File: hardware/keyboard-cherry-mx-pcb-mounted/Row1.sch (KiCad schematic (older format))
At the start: 30 parts, among them SW15 `, SW16 8, SW17 1, SW18 9, SW19 2, SW20 0, SW21 3, SW22 -, SW23 4, SW24 =, SW25 5, SW26 Backspace, SW27 6, SW28 Home, SW29 7

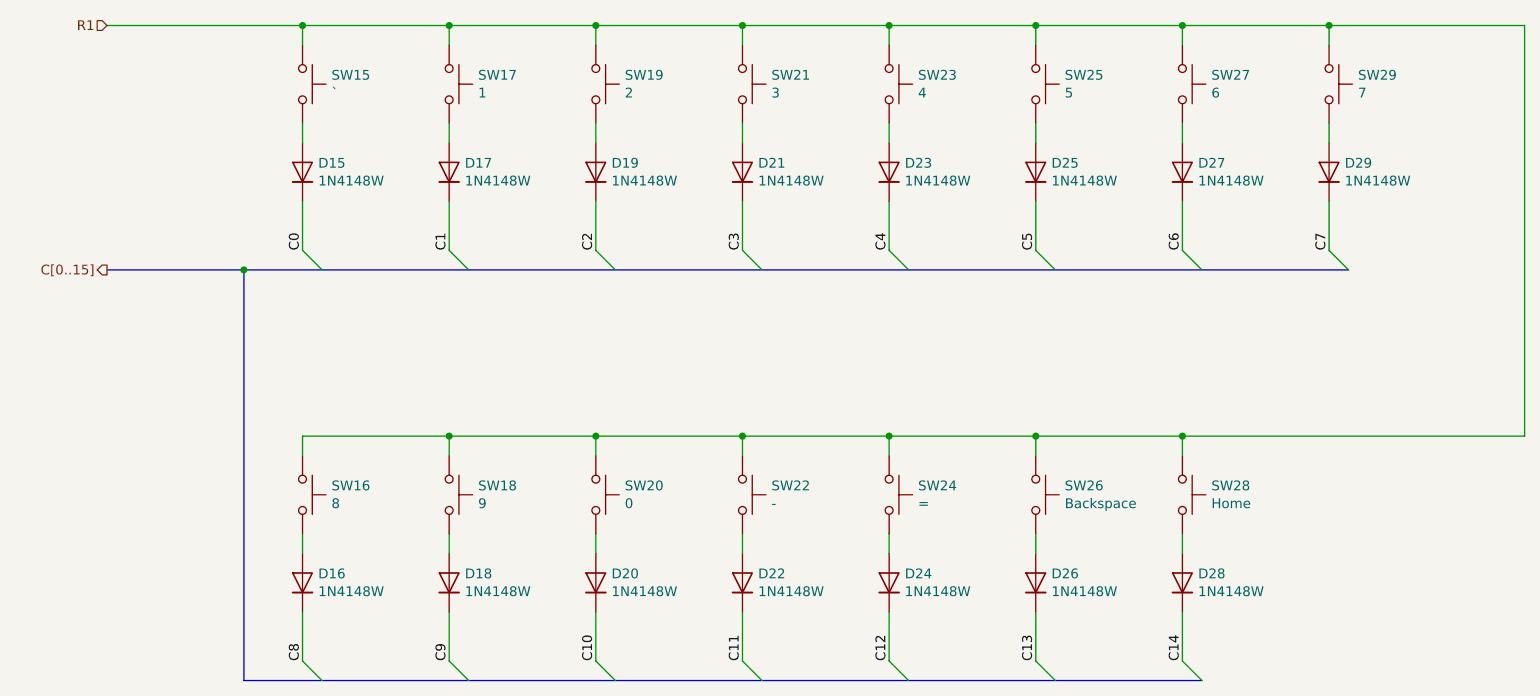
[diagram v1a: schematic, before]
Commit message: Adds completed sensor and power connections. Still need to add USB footprint then sch are done for version 1.0
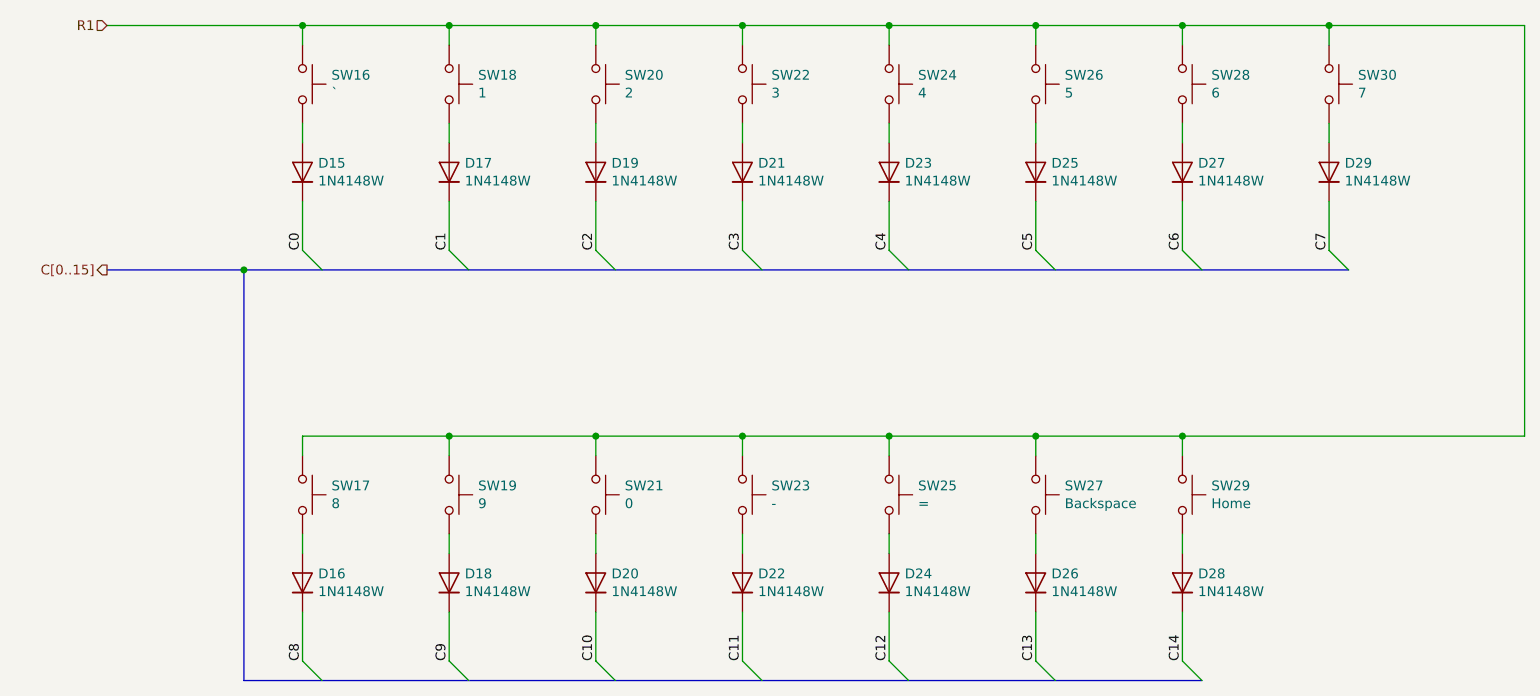
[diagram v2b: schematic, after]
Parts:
- renumbered SW15 to SW16, SW16 to SW17, SW17 to SW18, SW18 to SW19, SW19 to SW20, SW20 to SW21, SW21 to SW22, SW22 to SW23, SW23 to SW24, SW24 to SW25, SW25 to SW26, SW26 to SW27, SW27 to SW28, SW28 to SW29, SW29 to SW30
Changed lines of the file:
@@
 AR Path="/5E697948/5E775B33" Ref="SW?"  Part="1"
 AR Path="/5E697948/5E6CDE4B/5E775B33" Ref="SW?"  Part="1"
-AR Path="/5E697948/5E763FD4/5E775B33" Ref="SW15"  Part="1"
-F 0 "SW15" V 3154 2598 50  0000 L CNN
+AR Path="/5E697948/5E763FD4/5E775B33" Ref="SW16"  Part="1"
+F 0 "SW16" V 3154 2598 50  0000 L CNN
 F 1 "`" V 3245 2598 50  0000 L CNN
 F 2 "Button_Switch_Keyboard:SW_Cherry_MX_1.00u_PCB" H 3200 2650 50  0001 C CNN
@@
 AR Path="/5E697948/5E775B43" Ref="SW?"  Part="1"
 AR Path="/5E697948/5E6CDE4B/5E775B43" Ref="SW?"  Part="1"
-AR Path="/5E697948/5E763FD4/5E775B43" Ref="SW17"  Part="1"
-F 0 "SW17" V 3904 2598 50  0000 L CNN
+AR Path="/5E697948/5E763FD4/5E775B43" Ref="SW18"  Part="1"
+F 0 "SW18" V 3904 2598 50  0000 L CNN
 F 1 "1" V 3995 2598 50  0000 L CNN
 F 2 "Button_Switch_Keyboard:SW_Cherry_MX_1.00u_PCB" H 3950 2650 50  0001 C CNN
@@
 AR Path="/5E697948/5E775B51" Ref="SW?"  Part="1"
 AR Path="/5E697948/5E6CDE4B/5E775B51" Ref="SW?"  Part="1"
-AR Path="/5E697948/5E763FD4/5E775B51" Ref="SW19"  Part="1"
-F 0 "SW19" V 4654 2598 50  0000 L CNN
+AR Path="/5E697948/5E763FD4/5E775B51" Ref="SW20"  Part="1"
+F 0 "SW20" V 4654 2598 50  0000 L CNN
 F 1 "2" V 4745 2598 50  0000 L CNN
 F 2 "Button_Switch_Keyboard:SW_Cherry_MX_1.00u_PCB" H 4700 2650 50  0001 C CNN
@@
 AR Path="/5E697948/5E775B5F" Ref="SW?"  Part="1"
 AR Path="/5E697948/5E6CDE4B/5E775B5F" Ref="SW?"  Part="1"
-AR Path="/5E697948/5E763FD4/5E775B5F" Ref="SW21"  Part="1"
-F 0 "SW21" V 5404 2598 50  0000 L CNN
+AR Path="/5E697948/5E763FD4/5E775B5F" Ref="SW22"  Part="1"
+F 0 "SW22" V 5404 2598 50  0000 L CNN
 F 1 "3" V 5495 2598 50  0000 L CNN
 F 2 "Button_Switch_Keyboard:SW_Cherry_MX_1.00u_PCB" H 5450 2650 50  0001 C CNN
@@
 AR Path="/5E697948/5E775B6D" Ref="SW?"  Part="1"
 AR Path="/5E697948/5E6CDE4B/5E775B6D" Ref="SW?"  Part="1"
-AR Path="/5E697948/5E763FD4/5E775B6D" Ref="SW23"  Part="1"
-F 0 "SW23" V 6154 2598 50  0000 L CNN
+AR Path="/5E697948/5E763FD4/5E775B6D" Ref="SW24"  Part="1"
+F 0 "SW24" V 6154 2598 50  0000 L CNN
 F 1 "4" V 6245 2598 50  0000 L CNN
 F 2 "Button_Switch_Keyboard:SW_Cherry_MX_1.00u_PCB" H 6200 2650 50  0001 C CNN
@@
 AR Path="/5E697948/5E775B7B" Ref="SW?"  Part="1"
 AR Path="/5E697948/5E6CDE4B/5E775B7B" Ref="SW?"  Part="1"
-AR Path="/5E697948/5E763FD4/5E775B7B" Ref="SW25"  Part="1"
-F 0 "SW25" V 6904 2598 50  0000 L CNN
+AR Path="/5E697948/5E763FD4/5E775B7B" Ref="SW26"  Part="1"
+F 0 "SW26" V 6904 2598 50  0000 L CNN
 F 1 "5" V 6995 2598 50  0000 L CNN
 F 2 "Button_Switch_Keyboard:SW_Cherry_MX_1.00u_PCB" H 6950 2650 50  0001 C CNN
@@
 AR Path="/5E697948/5E775B89" Ref="SW?"  Part="1"
 AR Path="/5E697948/5E6CDE4B/5E775B89" Ref="SW?"  Part="1"
-AR Path="/5E697948/5E763FD4/5E775B89" Ref="SW27"  Part="1"
-F 0 "SW27" V 7654 2598 50  0000 L CNN
+AR Path="/5E697948/5E763FD4/5E775B89" Ref="SW28"  Part="1"
+F 0 "SW28" V 7654 2598 50  0000 L CNN
 F 1 "6" V 7745 2598 50  0000 L CNN
 F 2 "Button_Switch_Keyboard:SW_Cherry_MX_1.00u_PCB" H 7700 2650 50  0001 C CNN
@@
 AR Path="/5E697948/5E775B97" Ref="SW?"  Part="1"
 AR Path="/5E697948/5E6CDE4B/5E775B97" Ref="SW?"  Part="1"
-AR Path="/5E697948/5E763FD4/5E775B97" Ref="SW29"  Part="1"
-F 0 "SW29" V 8404 2598 50  0000 L CNN
+AR Path="/5E697948/5E763FD4/5E775B97" Ref="SW30"  Part="1"
+F 0 "SW30" V 8404 2598 50  0000 L CNN
 F 1 "7" V 8495 2598 50  0000 L CNN
 F 2 "Button_Switch_Keyboard:SW_Cherry_MX_1.00u_PCB" H 8450 2650 50  0001 C CNN
@@
 AR Path="/5E697948/5E775BA5" Ref="SW?"  Part="1"
 AR Path="/5E697948/5E6CDE4B/5E775BA5" Ref="SW?"  Part="1"
-AR Path="/5E697948/5E763FD4/5E775BA5" Ref="SW16"  Part="1"
-F 0 "SW16" V 3154 4698 50  0000 L CNN
+AR Path="/5E697948/5E763FD4/5E775BA5" Ref="SW17"  Part="1"
+F 0 "SW17" V 3154 4698 50  0000 L CNN
 F 1 "8" V 3245 4698 50  0000 L CNN
 F 2 "Button_Switch_Keyboard:SW_Cherry_MX_1.00u_PCB" H 3200 4750 50  0001 C CNN
@@
 AR Path="/5E697948/5E775BB3" Ref="SW?"  Part="1"
 AR Path="/5E697948/5E6CDE4B/5E775BB3" Ref="SW?"  Part="1"
-AR Path="/5E697948/5E763FD4/5E775BB3" Ref="SW18"  Part="1"
-F 0 "SW18" V 3904 4698 50  0000 L CNN
+AR Path="/5E697948/5E763FD4/5E775BB3" Ref="SW19"  Part="1"
+F 0 "SW19" V 3904 4698 50  0000 L CNN
 F 1 "9" V 3995 4698 50  0000 L CNN
 F 2 "Button_Switch_Keyboard:SW_Cherry_MX_1.00u_PCB" H 3950 4750 50  0001 C CNN
@@
 AR Path="/5E697948/5E775BC1" Ref="SW?"  Part="1"
 AR Path="/5E697948/5E6CDE4B/5E775BC1" Ref="SW?"  Part="1"
-AR Path="/5E697948/5E763FD4/5E775BC1" Ref="SW20"  Part="1"
-F 0 "SW20" V 4654 4698 50  0000 L CNN
+AR Path="/5E697948/5E763FD4/5E775BC1" Ref="SW21"  Part="1"
+F 0 "SW21" V 4654 4698 50  0000 L CNN
 F 1 "0" V 4745 4698 50  0000 L CNN
 F 2 "Button_Switch_Keyboard:SW_Cherry_MX_1.00u_PCB" H 4700 4750 50  0001 C CNN
@@
 AR Path="/5E697948/5E775BCF" Ref="SW?"  Part="1"
 AR Path="/5E697948/5E6CDE4B/5E775BCF" Ref="SW?"  Part="1"
-AR Path="/5E697948/5E763FD4/5E775BCF" Ref="SW22"  Part="1"
-F 0 "SW22" V 5404 4698 50  0000 L CNN
+AR Path="/5E697948/5E763FD4/5E775BCF" Ref="SW23"  Part="1"
+F 0 "SW23" V 5404 4698 50  0000 L CNN
 F 1 "-" V 5495 4698 50  0000 L CNN
 F 2 "Button_Switch_Keyboard:SW_Cherry_MX_1.00u_PCB" H 5450 4750 50  0001 C CNN
@@
 AR Path="/5E697948/5E775BDD" Ref="SW?"  Part="1"
 AR Path="/5E697948/5E6CDE4B/5E775BDD" Ref="SW?"  Part="1"
-AR Path="/5E697948/5E763FD4/5E775BDD" Ref="SW24"  Part="1"
-F 0 "SW24" V 6154 4698 50  0000 L CNN
+AR Path="/5E697948/5E763FD4/5E775BDD" Ref="SW25"  Part="1"
+F 0 "SW25" V 6154 4698 50  0000 L CNN
 F 1 "=" V 6245 4698 50  0000 L CNN
 F 2 "Button_Switch_Keyboard:SW_Cherry_MX_1.00u_PCB" H 6200 4750 50  0001 C CNN
@@
 AR Path="/5E697948/5E775BEB" Ref="SW?"  Part="1"
 AR Path="/5E697948/5E6CDE4B/5E775BEB" Ref="SW?"  Part="1"
-AR Path="/5E697948/5E763FD4/5E775BEB" Ref="SW26"  Part="1"
-F 0 "SW26" V 6904 4698 50  0000 L CNN
+AR Path="/5E697948/5E763FD4/5E775BEB" Ref="SW27"  Part="1"
+F 0 "SW27" V 6904 4698 50  0000 L CNN
 F 1 "Backspace" V 6995 4698 50  0000 L CNN
 F 2 "Button_Switch_Keyboard:SW_Cherry_MX_2.00u_PCB" H 6950 4750 50  0001 C CNN
@@
 AR Path="/5E697948/5E775BF9" Ref="SW?"  Part="1"
 AR Path="/5E697948/5E6CDE4B/5E775BF9" Ref="SW?"  Part="1"
-AR Path="/5E697948/5E763FD4/5E775BF9" Ref="SW28"  Part="1"
-F 0 "SW28" V 7654 4698 50  0000 L CNN
+AR Path="/5E697948/5E763FD4/5E775BF9" Ref="SW29"  Part="1"
+F 0 "SW29" V 7654 4698 50  0000 L CNN
 F 1 "Home" V 7745 4698 50  0000 L CNN
 F 2 "Button_Switch_Keyboard:SW_Cherry_MX_1.00u_PCB" H 7700 4750 50  0001 C CNN

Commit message: Aligns the keys so the column connections are more consistent. e.g. right most keys will have same column connection.
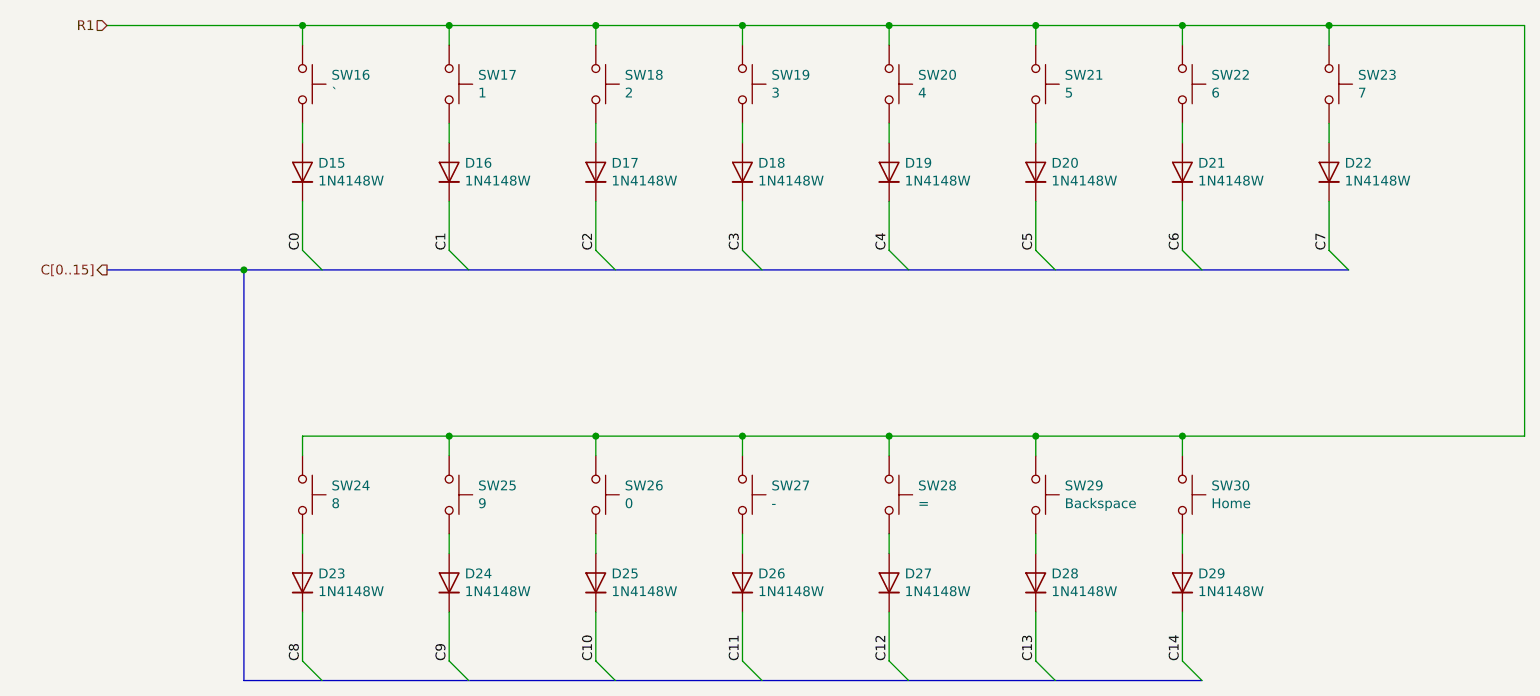
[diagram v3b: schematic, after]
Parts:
- renumbered D17 to D16, D19 to D17, D21 to D18, D23 to D19, D25 to D20, D27 to D21, D29 to D22, D16 to D23, D18 to D24, D20 to D25, D22 to D26, D24 to D27, D26 to D28, D28 to D29, SW18 to SW17, SW20 to SW18, SW22 to SW19, SW24 to SW20, SW26 to SW21, SW28 to SW22, SW30 to SW23, SW17 to SW24, SW19 to SW25, SW21 to SW26, SW23 to SW27, SW25 to SW28, SW27 to SW29, SW29 to SW30

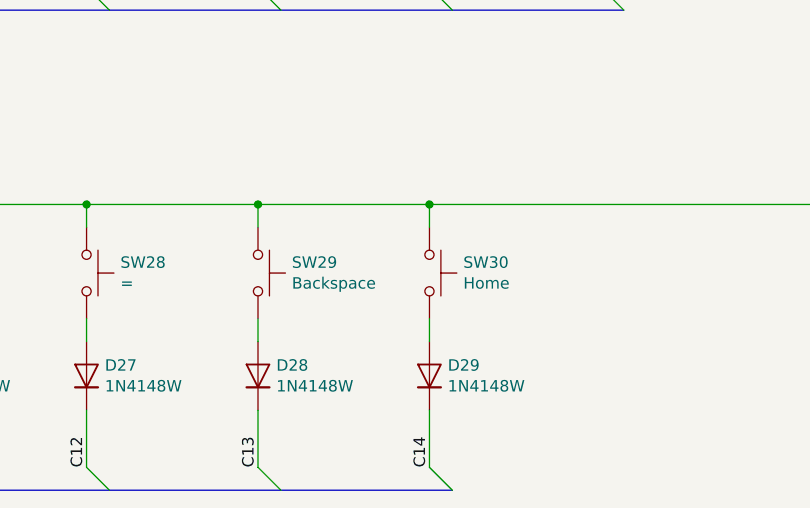
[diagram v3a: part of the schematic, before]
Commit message: Adds labels for each key and creates gerber files.
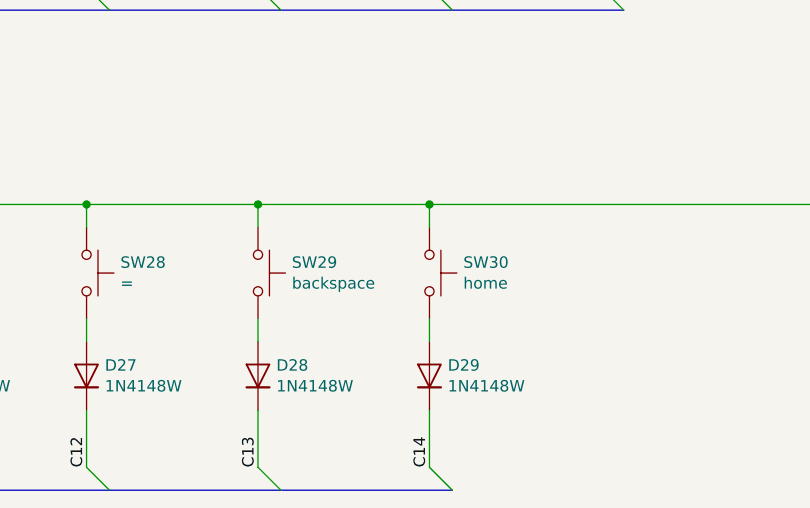
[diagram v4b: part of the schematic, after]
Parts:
- SW29: value Backspace -> backspace
- SW30: value Home -> home
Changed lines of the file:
@@
 AR Path="/5E697948/5E763FD4/5E775BEB" Ref="SW29"  Part="1"
 F 0 "SW29" V 6904 4698 50  0000 L CNN
-F 1 "Backspace" V 6995 4698 50  0000 L CNN
+F 1 "backspace" V 6995 4698 50  0000 L CNN
 F 2 "Button_Switch_Keyboard:SW_Cherry_MX_2.00u_PCB" H 6950 4750 50  0001 C CNN
 F 3 "~" H 6950 4750 50  0001 C CNN
@@
 AR Path="/5E697948/5E763FD4/5E775BF9" Ref="SW30"  Part="1"
 F 0 "SW30" V 7654 4698 50  0000 L CNN
-F 1 "Home" V 7745 4698 50  0000 L CNN
+F 1 "home" V 7745 4698 50  0000 L CNN
 F 2 "Button_Switch_Keyboard:SW_Cherry_MX_1.00u_PCB" H 7700 4750 50  0001 C CNN
 F 3 "~" H 7700 4750 50  0001 C CNN
